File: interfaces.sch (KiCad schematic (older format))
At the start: 17 parts, among them U10 TDA19988BHN_C1,557

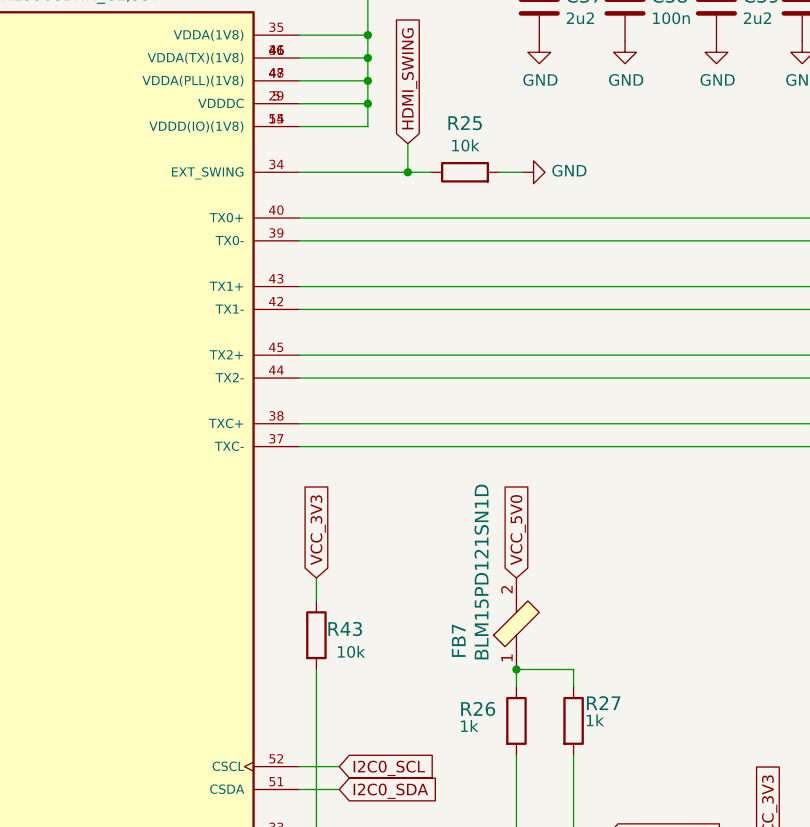
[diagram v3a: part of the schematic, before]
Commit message: Updated component placement - HDMI IC passives, QSPI, 5V8 buck placed
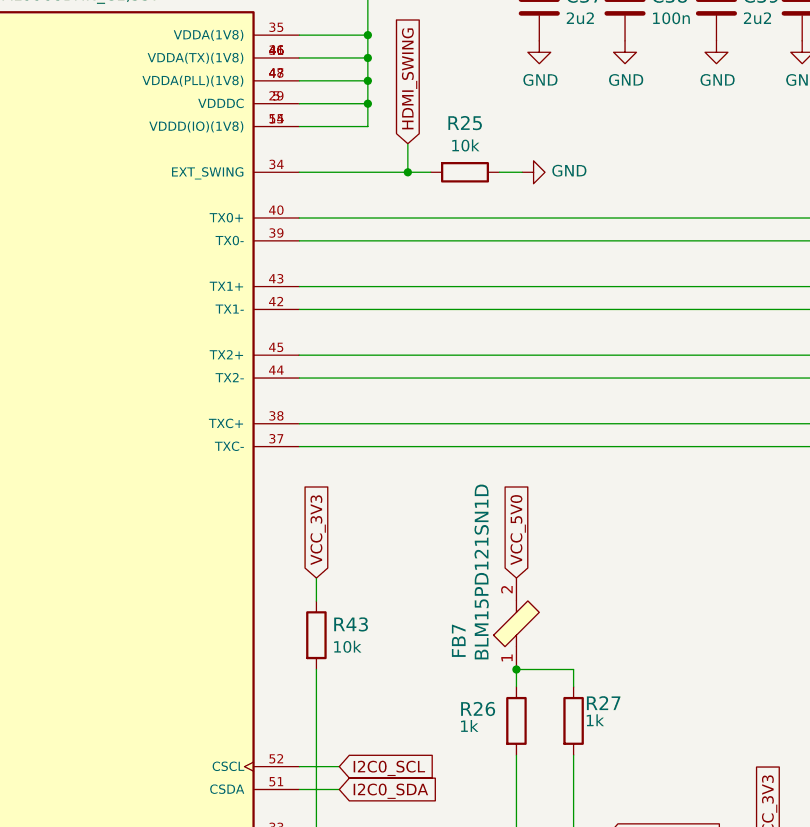
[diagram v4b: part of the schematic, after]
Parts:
- removed R25, R43: R_10k_0402, arvsom-footprints:0402-res, symbol arvsom:R_10k_0402
- added R25, R43: R_10k_0201, arvsom-footprints:0201-res, symbol arvsom:R_10k_0201
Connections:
- net GND: now also R25.1
- net HDMI_INT: now also R43.2
- net HDMI_SWING: now also R25.2
- net VCC_3V3: now also R43.1
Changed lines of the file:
@@
 Comment4 ""
 $EndDescr
-$Comp
-L arvsom:TDA19988BHN_C1,557 U10
-U 1 1 607A5735
-P 7075 5525
-F 0 "U10" H 7075 8192 50  0000 C CNN
-F 1 "TDA19988BHN_C1,557" H 7075 8101 50  0000 C CNN
-F 2 "arvsom-footprints:QFN50P900X900X100-65N" H 7075 5525 50  0001 L BNN
-F 3 "" H 7075 5525 50  0001 L BNN
-F 4 "NXP Semiconductors" H 7075 5525 50  0001 L BNN "MANUFACTURER"
-F 5 "1.0 mm" H 7075 5525 50  0001 L BNN "MAXIMUM_PACKAGE_HEIGHT"
-F 6 "IPC 7351B" H 7075 5525 50  0001 L BNN "STANDARD"
-F 7 "3" H 7075 5525 50  0001 L BNN "PARTREV"
-	1    7075 5525
-	1    0    0    -1
-$EndComp
 Text Notes 6300 2100 0    118  ~ 24
 HDMI transmitter
@@
 	8550 3725 8650 3725
 $Comp
-L arvsom:R_10k_0402 R25
-U 1 1 608924F4
-P 8800 3725
-F 0 "R25" H 8800 3938 60  0000 C CNN
-F 1 "R_10k_0402" H 8800 3575 60  0001 C CNN
-F 2 "arvsom-footprints:0402-res" H 9000 3925 60  0001 L CNN
-F 3 "" H 8800 3725 50  0001 C CNN
-F 4 "VISHAY" H 9000 4125 60  0001 L CNN "Manufacturer"
-F 5 "CRCW040210K0FKEDHP" H 9000 4025 60  0001 L CNN "MPN"
-F 6 "10k" H 8800 3840 50  0000 C CNN "Val"
-	1    8800 3725
-	1    0    0    -1
-$EndComp
-$Comp
 L arvsom:GND #PWR0146
 U 1 1 60893600
@@
 HDMI_TXC_N
 Wire Wire Line
-	8075 4025 10500 4025
-Wire Wire Line
 	8075 4225 10500 4225
 Wire Wire Line
-	8075 4325 10500 4325
-Wire Wire Line
 	8075 4525 10500 4525
 Wire Wire Line
-	8075 4625 10500 4625
-Wire Wire Line
 	8075 4825 10500 4825
 Wire Wire Line
@@
 Connection ~ 9025 6725
 Wire Wire Line
-	9025 6725 9425 6725
-Wire Wire Line
 	9275 6275 9275 6625
 Connection ~ 9275 6625
@@
 Wire Wire Line
 	9025 5900 9025 5975
-Wire Wire Line
-	8075 7325 9425 7325
 Text GLabel 9425 7325 2    50   Input ~ 0
 HDMI_HPD
@@
 	8950 6950 8950 7125
 Connection ~ 8950 7125
-Wire Wire Line
-	8950 7125 9425 7125
 $Comp
 L arvsom:R_27k_0402 R28
@@
 Wire Wire Line
 	8275 6925 8150 6925
-$Comp
-L arvsom:R_10k_0402 R43
-U 1 1 6095B9AC
-P 8150 5750
-F 0 "R43" V 8125 5875 60  0000 C CNN
-F 1 "R_10k_0402" H 8150 5600 60  0001 C CNN
-F 2 "arvsom-footprints:0402-res" H 8350 5950 60  0001 L CNN
-F 3 "" H 8150 5750 50  0001 C CNN
-F 4 "VISHAY" H 8350 6150 60  0001 L CNN "Manufacturer"
-F 5 "CRCW040210K0FKEDHP" H 8350 6050 60  0001 L CNN "MPN"
-F 6 "10k" V 8225 5900 50  0000 C CNN "Val"
-	1    8150 5750
-	0    1    1    0
-$EndComp
 Text GLabel 8150 5500 1    50   Input ~ 0
 VCC_3V3
@@
 Wire Wire Line
 	8150 6925 8075 6925
+Wire Wire Line
+	9025 6725 9425 6725
+Wire Wire Line
+	8075 7325 9425 7325
+Wire Wire Line
+	8075 4325 10500 4325
+Wire Wire Line
+	8075 4025 10500 4025
+Wire Wire Line
+	8075 4625 10500 4625
+Wire Wire Line
+	8950 7125 9425 7125
+$Comp
+L arvsom:TDA19988BHN_C1,557 U10
+U 1 1 607A5735
+P 7075 5525
+F 0 "U10" H 7075 8192 50  0000 C CNN
+F 1 "TDA19988BHN_C1,557" H 7075 8101 50  0000 C CNN
+F 2 "arvsom-footprints:QFN50P900X900X100-65N" H 7075 5525 50  0001 L BNN
+F 3 "" H 7075 5525 50  0001 L BNN
+F 4 "NXP Semiconductors" H 7075 5525 50  0001 L BNN "MANUFACTURER"
+F 5 "1.0 mm" H 7075 5525 50  0001 L BNN "MAXIMUM_PACKAGE_HEIGHT"
+F 6 "IPC 7351B" H 7075 5525 50  0001 L BNN "STANDARD"
+F 7 "3" H 7075 5525 50  0001 L BNN "PARTREV"
+	1    7075 5525
+	1    0    0    -1
+$EndComp
+$Comp
+L arvsom:R_10k_0201 R43
+U 1 1 60C0ABE2
+P 8150 5750
+F 0 "R43" V 8105 5820 60  0000 L CNN
+F 1 "R_10k_0201" H 8150 5600 60  0001 C CNN
+F 2 "arvsom-footprints:0201-res" H 8350 5950 60  0001 L CNN
+F 3 "" H 8150 5750 50  0001 C CNN
+F 4 "YAGEO" H 8350 6150 60  0001 L CNN "Manufacturer"
+F 5 "RC0201FR-0710KL" H 8350 6050 60  0001 L CNN "MPN"
+F 6 "10k" V 8203 5820 50  0000 L CNN "Val"
+	1    8150 5750
+	0    1    1    0
+$EndComp
+$Comp
+L arvsom:R_10k_0201 R25
+U 1 1 60C10088
+P 8800 3725
+F 0 "R25" H 8800 3512 60  0000 C CNN
+F 1 "R_10k_0201" H 8800 3575 60  0001 C CNN
+F 2 "arvsom-footprints:0201-res" H 9000 3925 60  0001 L CNN
+F 3 "" H 8800 3725 50  0001 C CNN
+F 4 "YAGEO" H 9000 4125 60  0001 L CNN "Manufacturer"
+F 5 "RC0201FR-0710KL" H 9000 4025 60  0001 L CNN "MPN"
+F 6 "10k" H 8800 3610 50  0000 C CNN "Val"
+	1    8800 3725
+	-1   0    0    1
+$EndComp
 $EndSCHEMATC

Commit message: Update lib attributes
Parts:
- U8: renamed from U10; MANUFACTURER NXP Semiconductors -> (none); MAXIMUM_PACKAGE_HEIGHT 1.0 mm -> (none); MPN (none) -> TDA19988BHN_C1,557; Manufacturer (none) -> NXP Semiconductors; PARTREV 3 -> (none); STANDARD IPC 7351B -> (none)
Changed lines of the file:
@@
 	8950 7125 9425 7125
 $Comp
-L arvsom:TDA19988BHN_C1,557 U10
+L arvsom:TDA19988BHN_C1,557 U8
 U 1 1 607A5735
 P 7075 5525
-F 0 "U10" H 7075 8192 50  0000 C CNN
+F 0 "U8" H 7075 8192 50  0000 C CNN
 F 1 "TDA19988BHN_C1,557" H 7075 8101 50  0000 C CNN
 F 2 "arvsom-footprints:QFN50P900X900X100-65N" H 7075 5525 50  0001 L BNN
 F 3 "" H 7075 5525 50  0001 L BNN
-F 4 "NXP Semiconductors" H 7075 5525 50  0001 L BNN "MANUFACTURER"
-F 5 "1.0 mm" H 7075 5525 50  0001 L BNN "MAXIMUM_PACKAGE_HEIGHT"
-F 6 "IPC 7351B" H 7075 5525 50  0001 L BNN "STANDARD"
-F 7 "3" H 7075 5525 50  0001 L BNN "PARTREV"
+F 4 "TDA19988BHN_C1,557" H 7075 5525 50  0001 C CNN "MPN"
+F 5 "NXP Semiconductors" H 7075 5525 50  0001 C CNN "Manufacturer"
 	1    7075 5525
 	1    0    0    -1
